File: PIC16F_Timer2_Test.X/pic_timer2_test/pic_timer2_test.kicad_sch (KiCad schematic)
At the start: 15 parts, among them J1 To Analog Discovery 2, SW2 SW_Push, U1 PIC16F877A-IP, U2 BA50JC5, Y1 Crystal

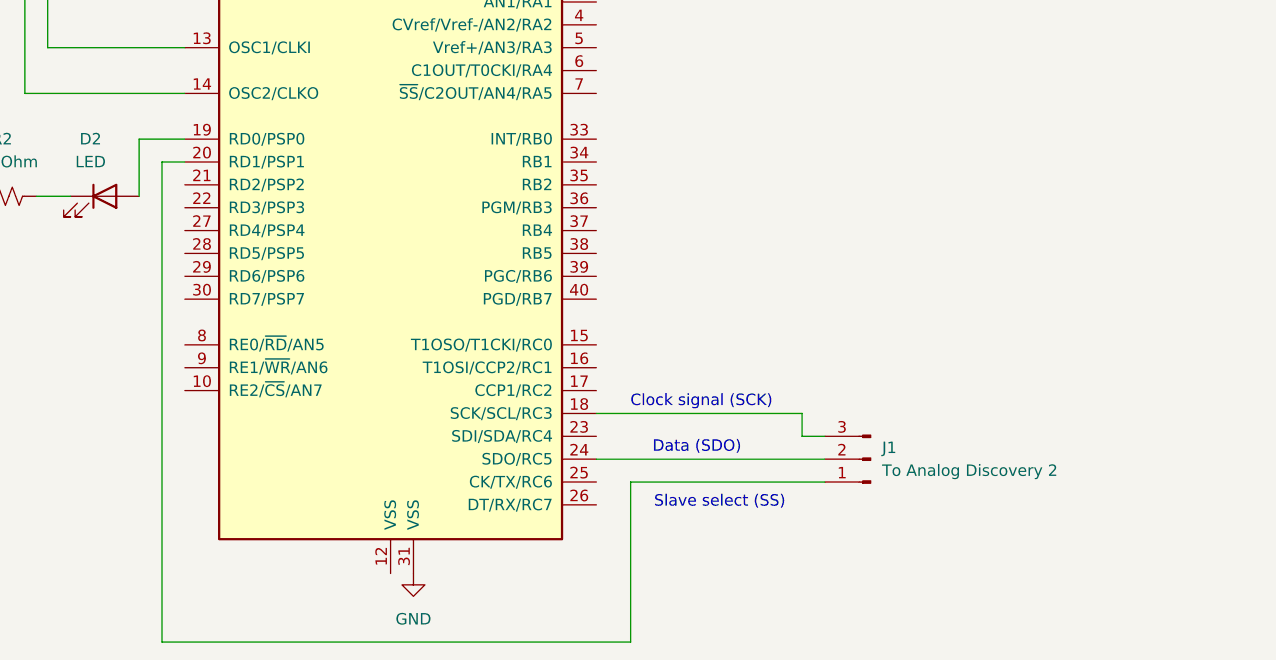
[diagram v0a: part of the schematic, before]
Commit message: updated the Timer2 project schematic to match the circuit
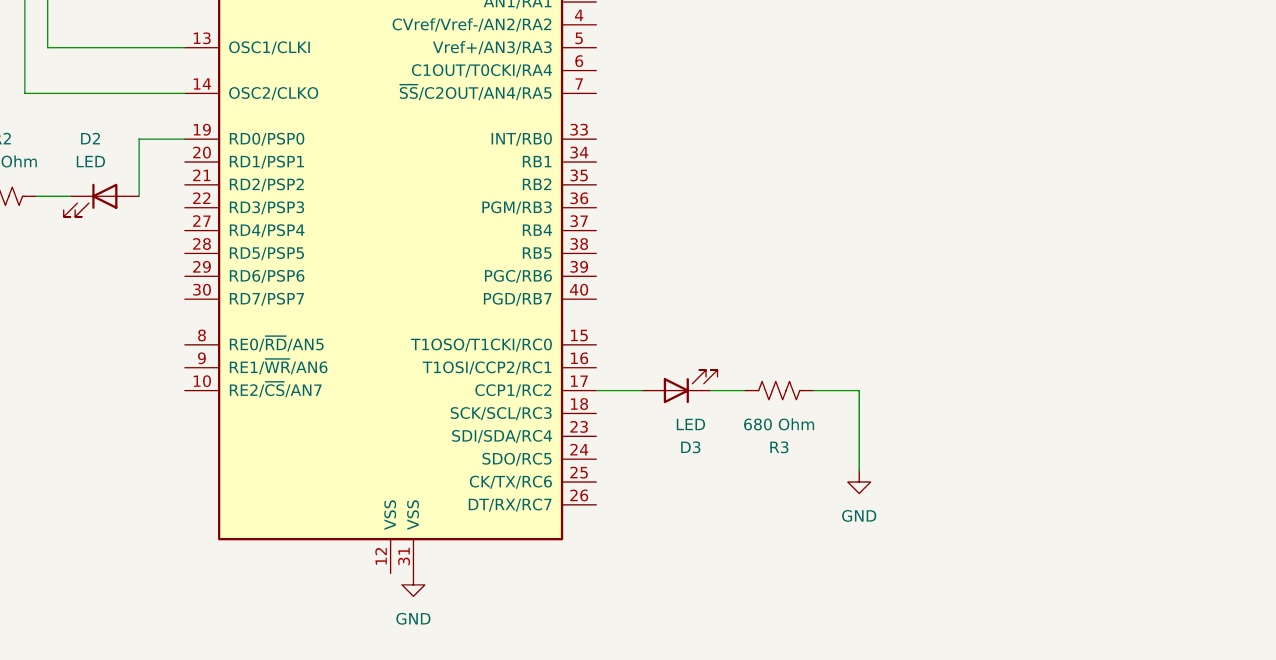
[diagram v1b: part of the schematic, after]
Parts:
- removed J1: To Analog Discovery 2, symbol Connector:Conn_01x03_Pin
- added D3: LED, symbol Device:LED
- added R3: 680 Ohm, symbol Device:R_US
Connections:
- net GND: now also R3.1
- net at U1.17 (CCP1/RC2): now also D3.2 (A)
- new net: D3.1 (K), R3.2
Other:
- note removed: "Clock signal (SCK)"
- note removed: "Data (SDO)"
- note removed: "Slave select (SS)"
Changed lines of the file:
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@@
 	(generator_version "9.0")
 	(paper "A4")
-	(text "Clock signal (SCK)"
-		(exclude_from_sim no)
-		(at 179.324 115.57 0)
-		(effects
-			(font
-				(size 1.27 1.27)
-			)
-		)
-	)
-	(text "Data (SDO)"
-		(exclude_from_sim no)
-		(at 178.816 120.65 0)
-		(effects
-			(font
-				(size 1.27 1.27)
-			)
-		)
-	)
-	(text "Slave select (SS)"
-		(exclude_from_sim no)
-		(at 181.356 126.746 0)
-		(effects
-			(font
-				(size 1.27 1.27)
-			)
-		)
-	)
 	(junction
 		(at 212.09 33.02)
@@
 	(wire
 		(pts
-			(xy 171.45 142.24) (xy 171.45 124.46)
+			(xy 196.85 114.3) (xy 196.85 123.19)
 		)
 		(stroke
@@
 	(wire
 		(pts
-			(xy 193.04 119.38) (xy 190.5 119.38)
+			(xy 184.15 114.3) (xy 180.34 114.3)
 		)
 		(stroke
@@
 	(wire
 		(pts
+			(xy 167.64 114.3) (xy 172.72 114.3)
+		)
+		(stroke
+			(width 0)
+			(type default)
+		)
+	)
+	(wire
+		(pts
 			(xy 147.32 52.07) (xy 151.13 52.07)
 		)
@@
 	(wire
 		(pts
+			(xy 191.77 114.3) (xy 196.85 114.3)
+		)
+		(stroke
+			(width 0)
+			(type default)
+		)
+	)
+	(wire
+		(pts
 			(xy 116.84 86.36) (xy 116.84 92.71)
 		)
@@
 	(wire
 		(pts
-			(xy 171.45 124.46) (xy 193.04 124.46)
-		)
-		(stroke
-			(width 0)
-			(type default)
-		)
-	)
-	(wire
-		(pts
 			(xy 97.79 92.71) (xy 97.79 96.52)
 		)
@@
 	(wire
 		(pts
-			(xy 119.38 142.24) (xy 171.45 142.24)
-		)
-		(stroke
-			(width 0)
-			(type default)
-		)
-	)
-	(wire
-		(pts
-			(xy 167.64 121.92) (xy 193.04 121.92)
-		)
-		(stroke
-			(width 0)
-			(type default)
-		)
-	)
-	(wire
-		(pts
-			(xy 119.38 88.9) (xy 119.38 142.24)
-		)
-		(stroke
-			(width 0)
-			(type default)
-		)
-	)
-	(wire
-		(pts
 			(xy 104.14 68.58) (xy 104.14 81.28)
 		)
@@
 	(wire
 		(pts
-			(xy 121.92 88.9) (xy 119.38 88.9)
-		)
-		(stroke
-			(width 0)
-			(type default)
-		)
-	)
-	(wire
-		(pts
 			(xy 212.09 29.21) (xy 212.09 33.02)
 		)
@@
 	(wire
 		(pts
-			(xy 167.64 116.84) (xy 190.5 116.84)
-		)
-		(stroke
-			(width 0)
-			(type default)
-		)
-	)
-	(wire
-		(pts
 			(xy 242.57 33.02) (xy 246.38 33.02)
-		)
-		(stroke
-			(width 0)
-			(type default)
-		)
-	)
-	(wire
-		(pts
-			(xy 190.5 119.38) (xy 190.5 116.84)
 		)
 		(stroke
@@
 	)
 	(symbol
-		(lib_id "Connector:Conn_01x03_Pin")
-		(at 198.12 121.92 180)
-		(unit 1)
-		(exclude_from_sim no)
-		(in_bom yes)
-		(on_board yes)
-		(dnp no)
-		(fields_autoplaced yes)
-		(property "Reference" "J1"
-			(at 199.39 120.6499 0)
-			(effects
-				(font
-					(size 1.27 1.27)
-				)
-				(justify right)
-			)
-		)
-		(property "Value" "To Analog Discovery 2"
-			(at 199.39 123.1899 0)
-			(effects
-				(font
-					(size 1.27 1.27)
-				)
-				(justify right)
-			)
-		)
-		(property "Footprint" ""
-			(at 198.12 121.92 0)
+		(lib_id "Device:LED")
+		(at 176.53 114.3 180)
+		(unit 1)
+		(exclude_from_sim no)
+		(in_bom yes)
+		(on_board yes)
+		(dnp no)
+		(fields_autoplaced yes)
+		(property "Reference" "D3"
+			(at 178.1175 120.65 0)
+			(effects
+				(font
+					(size 1.27 1.27)
+				)
+			)
+		)
+		(property "Value" "LED"
+			(at 178.1175 118.11 0)
+			(effects
+				(font
+					(size 1.27 1.27)
+				)
+			)
+		)
+		(property "Footprint" ""
+			(at 176.53 114.3 0)
 			(effects
 				(font
@@
 		)
 		(property "Datasheet" "~"
-			(at 198.12 121.92 0)
-			(effects
-				(font
-					(size 1.27 1.27)
-				)
-				(hide yes)
-			)
-		)
-		(property "Description" "Generic connector, single row, 01x03, script generated"
-			(at 198.12 121.92 0)
-			(effects
-				(font
-					(size 1.27 1.27)
-				)
-				(hide yes)
-			)
-		)
-		(pin "1"
+			(at 176.53 114.3 0)
+			(effects
+				(font
+					(size 1.27 1.27)
+				)
+				(hide yes)
+			)
+		)
+		(property "Description" "Light emitting diode"
+			(at 176.53 114.3 0)
+			(effects
+				(font
+					(size 1.27 1.27)
+				)
+				(hide yes)
+			)
+		)
+		(property "Sim.Pins" "1=K 2=A"
+			(at 176.53 114.3 0)
+			(effects
+				(font
+					(size 1.27 1.27)
+				)
+				(hide yes)
+			)
 		)
 		(pin "2"
 		)
-		(pin "3"
-		)
-		(instances
-			(project ""
-				(path "/6ac39a3a-98e0-464c-968e-de313f68ebc4"
-					(reference "J1")
+		(pin "1"
+		)
+		(instances
+			(project "pic_timer2_test"
+				(path "/6ac39a3a-98e0-464c-968e-de313f68ebc4"
+					(reference "D3")
 					(unit 1)
 				)
@@
 	)
 	(symbol
+		(lib_id "Device:R_US")
+		(at 187.96 114.3 270)
+		(unit 1)
+		(exclude_from_sim no)
+		(in_bom yes)
+		(on_board yes)
+		(dnp no)
+		(fields_autoplaced yes)
+		(property "Reference" "R3"
+			(at 187.96 120.65 90)
+			(effects
+				(font
+					(size 1.27 1.27)
+				)
+			)
+		)
+		(property "Value" "680 Ohm"
+			(at 187.96 118.11 90)
+			(effects
+				(font
+					(size 1.27 1.27)
+				)
+			)
+		)
+		(property "Footprint" ""
+			(at 187.706 115.316 90)
+			(effects
+				(font
+					(size 1.27 1.27)
+				)
+				(hide yes)
+			)
+		)
+		(property "Datasheet" "~"
+			(at 187.96 114.3 0)
+			(effects
+				(font
+					(size 1.27 1.27)
+				)
+				(hide yes)
+			)
+		)
+		(property "Description" "Resistor, US symbol"
+			(at 187.96 114.3 0)
+			(effects
+				(font
+					(size 1.27 1.27)
+				)
+				(hide yes)
+			)
+		)
+		(pin "1"
+		)
+		(pin "2"
+		)
+		(instances
+			(project "pic_timer2_test"
+				(path "/6ac39a3a-98e0-464c-968e-de313f68ebc4"
+					(reference "R3")
+					(unit 1)
+				)
+			)
+		)
+	)
+	(symbol
 		(lib_id "Switch:SW_Push")
 		(at 105.41 44.45 270)
@@
 					(unit 1)
 				)
+			)
+		)
+	)
+	(symbol
+		(lib_id "power:GND")
+		(at 196.85 123.19 0)
+		(unit 1)
+		(exclude_from_sim no)
+		(in_bom yes)
+		(on_board yes)
+		(dnp no)
+		(fields_autoplaced yes)
+		(property "Reference" "#PWR012"
+			(at 196.85 129.54 0)
+			(effects
+				(font
+					(size 1.27 1.27)
+				)
+				(hide yes)
+			)
+		)
+		(property "Value" "GND"
+			(at 196.85 128.27 0)
+			(effects
+				(font
+					(size 1.27 1.27)
+				)
+			)
+		)
+		(property "Footprint" ""
+			(at 196.85 123.19 0)
+			(effects
+				(font
+					(size 1.27 1.27)
+				)
+				(hide yes)
+			)
+		)
+		(property "Datasheet" ""
+			(at 196.85 123.19 0)
+			(effects
+				(font
+					(size 1.27 1.27)
+				)
+				(hide yes)
+			)
+		)
+		(property "Description" "Power symbol creates a global label with name \"GND\" , ground"
+			(at 196.85 123.19 0)
+			(effects
+				(font
+					(size 1.27 1.27)
+				)
+				(hide yes)
+			)
+		)
+		(pin "1"
+		)
+		(instances
+			(project "pic_timer2_test"
+				(path "/6ac39a3a-98e0-464c-968e-de313f68ebc4"
+					(reference "#PWR012")
+					(unit 1)
+				)
